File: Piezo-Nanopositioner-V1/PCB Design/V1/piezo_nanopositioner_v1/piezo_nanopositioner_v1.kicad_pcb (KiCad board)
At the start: 2 copper layers, 34 parts, among them J101 Conn_01x03_Pin, J401 Conn_01x10_Pin, J402 RF2-04A-T-00-50-G, U401 TL431AIDBZR, U402 DAC0800LCM, U403 TDA2050

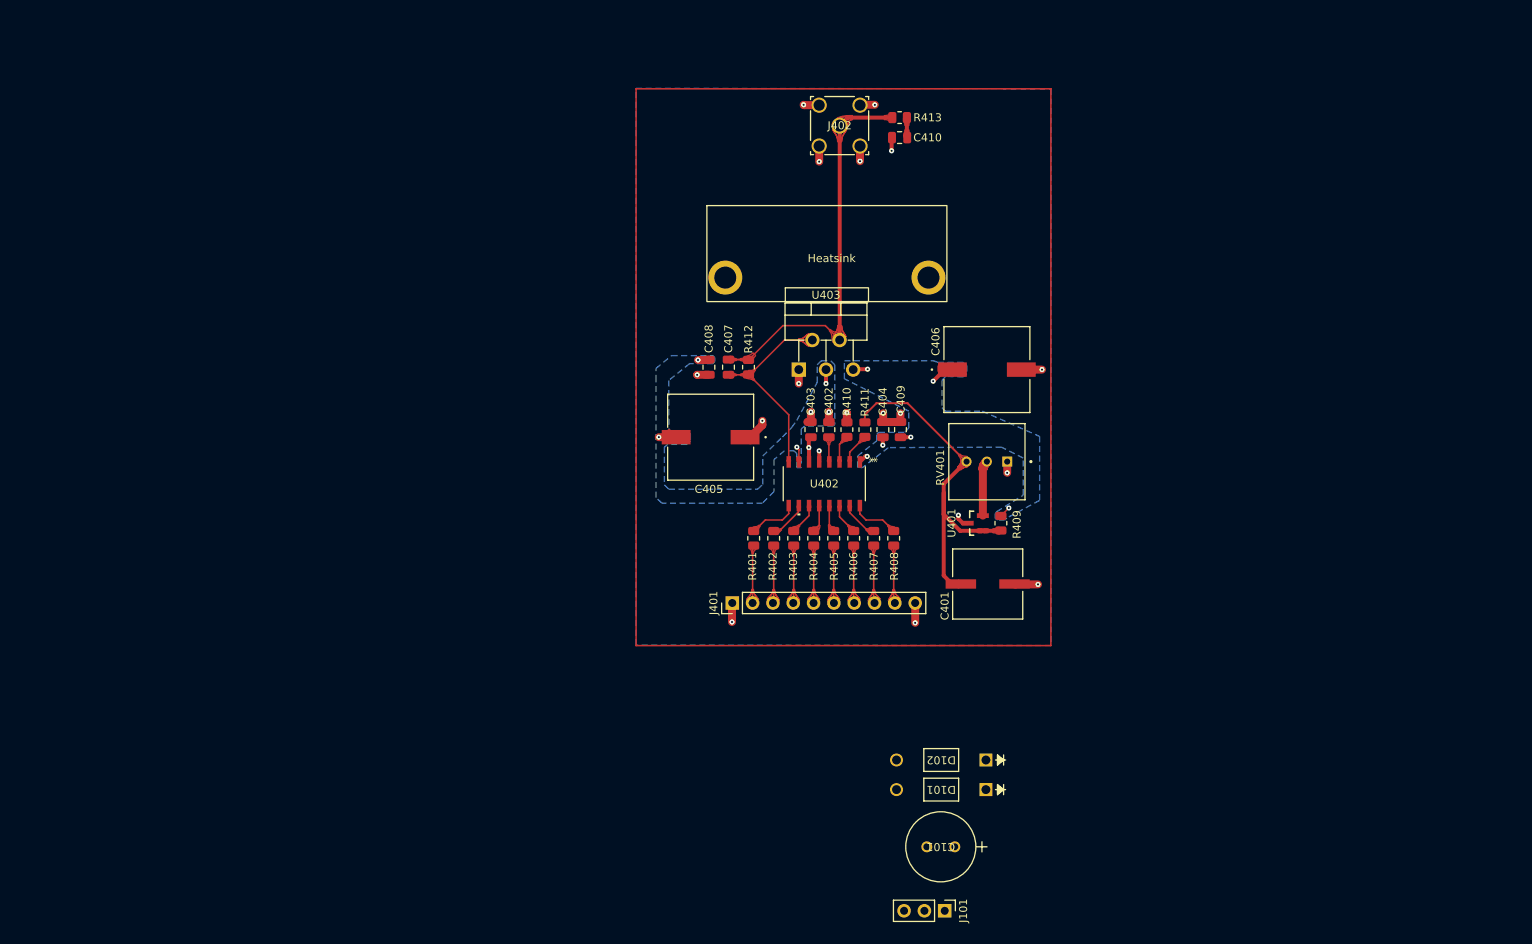
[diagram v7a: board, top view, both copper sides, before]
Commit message: Added 3d model files for component. Finished connecting the fill zones. Added mounting holes. Added pictures of pcb and layout.
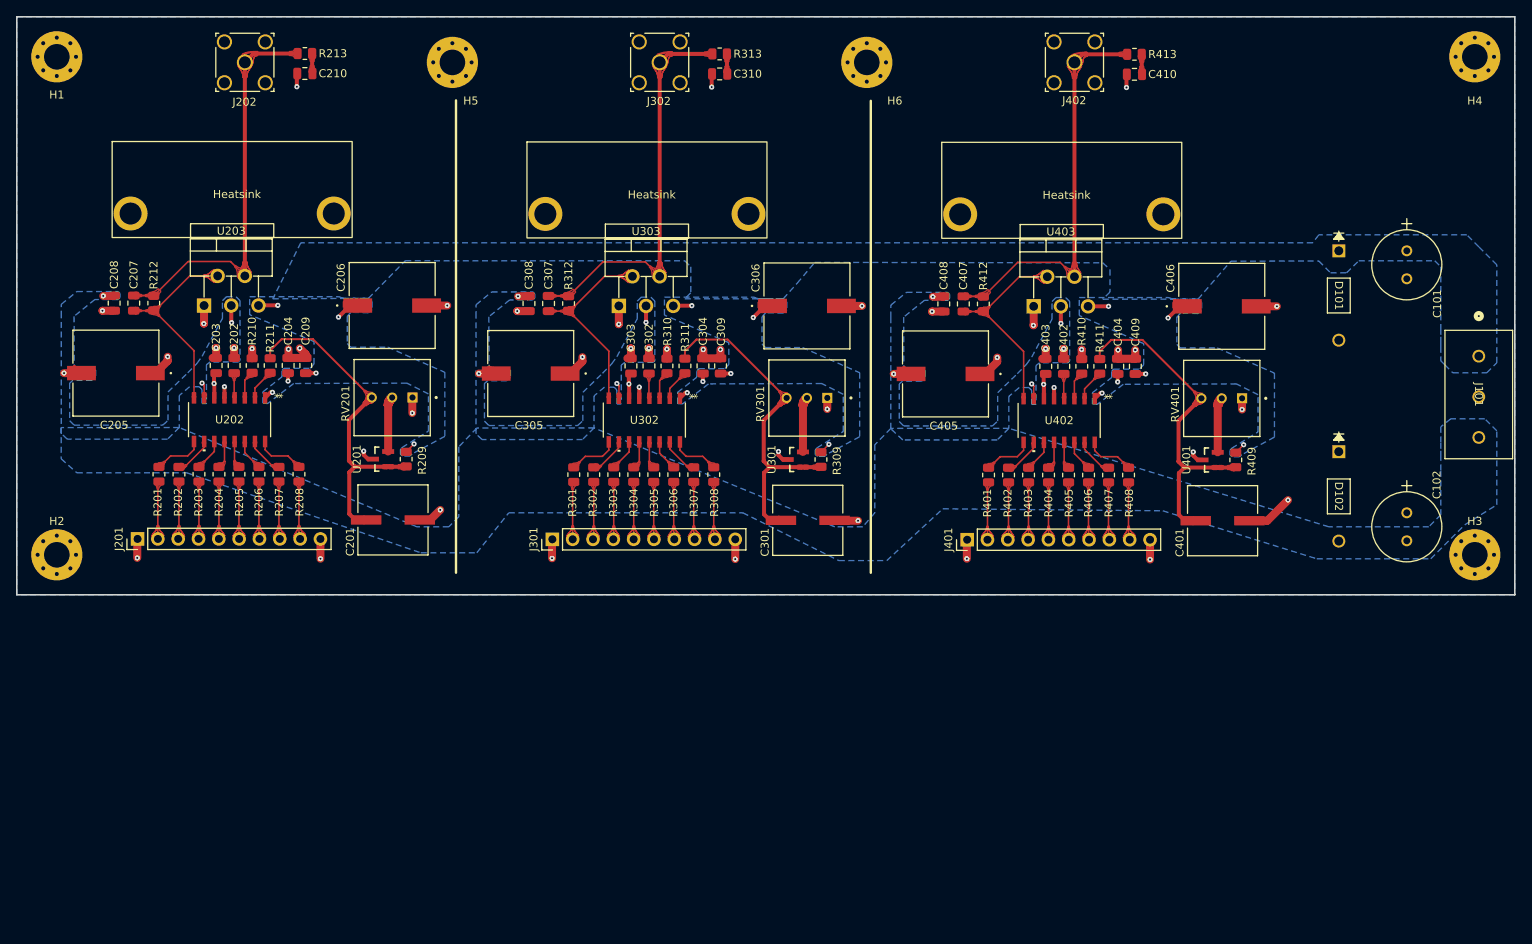
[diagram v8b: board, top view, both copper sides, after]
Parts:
- removed the Heatsink at (171.5, 76.1)
- added C102: 100uF 50V, Capacitor_THT:CAP_YX_8X11P5_RUB, F.Cu at (244.0, 105.5)
- added C201: 47u, Capacitor_SMD:CAP_EEFC_E_PAN, F.Cu at (117.3, 106.4)
- added C202: 10n, Capacitor_SMD:C_0805_2012Metric, F.Cu at (97.4, 87.1)
- added C203: 100n, Capacitor_SMD:C_0805_2012Metric, F.Cu at (95.2, 87.1)
- added C204: 100n, Capacitor_SMD:C_0805_2012Metric, F.Cu at (104.2, 87.1)
- added C205: 470u, Capacitor_THT:CAP_ZSU_G12_PAN, F.Cu at (82.6, 88.0)
- added C206: 470u, Capacitor_THT:CAP_ZSU_G12_PAN, F.Cu at (117.2, 79.6)
- added C207: 68p, Capacitor_SMD:C_0805_2012Metric, F.Cu at (84.9, 79.3)
- added C208: 100n, Capacitor_SMD:C_0805_2012Metric, F.Cu at (82.4, 79.3)
- added C209: 100n, Capacitor_SMD:C_0805_2012Metric, F.Cu at (106.4, 87.1)
- added C210: 4.7n, Capacitor_SMD:C_0805_2012Metric, F.Cu at (106.3, 50.6)
- added C301: 47u, Capacitor_SMD:CAP_EEFC_E_PAN, F.Cu at (169.1, 106.4)
- added C302: 10n, Capacitor_SMD:C_0805_2012Metric, F.Cu at (149.3, 87.1)
- added C303: 100n, Capacitor_SMD:C_0805_2012Metric, F.Cu at (147.0, 87.1)
- added C304: 100n, Capacitor_SMD:C_0805_2012Metric, F.Cu at (156.0, 87.1)
- added C305: 470u, Capacitor_THT:CAP_ZSU_G12_PAN, F.Cu at (134.5, 88.1)
- added C306: 470u, Capacitor_THT:CAP_ZSU_G12_PAN, F.Cu at (169.0, 79.6)
- added C307: 68p, Capacitor_SMD:C_0805_2012Metric, F.Cu at (136.7, 79.3)
- added C308: 100n, Capacitor_SMD:C_0805_2012Metric, F.Cu at (134.3, 79.3)
- added C309: 100n, Capacitor_SMD:C_0805_2012Metric, F.Cu at (158.2, 87.1)
- added C310: 4.7n, Capacitor_SMD:C_0805_2012Metric, F.Cu at (158.1, 50.6)
- added H1: MountingHole, MountingHole:MountingHole_3.2mm_M3_Pad_Via, F.Cu at (75.2, 48.5)
- added H2: MountingHole, MountingHole:MountingHole_3.2mm_M3_Pad_Via, F.Cu at (75.2, 110.8)
- added H3: MountingHole, MountingHole:MountingHole_3.2mm_M3_Pad_Via, F.Cu at (252.5, 110.8)
- added H4: MountingHole, MountingHole:MountingHole_3.2mm_M3_Pad_Via, F.Cu at (252.5, 48.5)
- added H5: MountingHole, MountingHole:MountingHole_3.2mm_M3_Pad_Via, F.Cu at (124.7, 49.2)
- added H6: MountingHole, MountingHole:MountingHole_3.2mm_M3_Pad_Via, F.Cu at (176.5, 49.2)
- added Heatsink: V6560Y, V6560Y:V6560Y, F.Cu at (200.9, 68.2)
- added Heatsink: V6560Y, V6560Y:V6560Y, F.Cu at (97.2, 68.1)
- added Heatsink: V6560Y, V6560Y:V6560Y, F.Cu at (149.0, 68.1)
- added J201: Conn_01x10_Pin, Connector_PinHeader_2.54mm:PinHeader_1x10_P2.54mm_Vertical, F.Cu at (85.3, 108.8)
- added J202: RF2-04A-T-00-50-G, RF:CONN_RF2-04A-T-00-50-G_ADM, F.Cu at (98.8, 49.2)
- added J301: Conn_01x10_Pin, Connector_PinHeader_2.54mm:PinHeader_1x10_P2.54mm_Vertical, F.Cu at (137.2, 108.8)
- added J302: RF2-04A-T-00-50-G, RF:CONN_RF2-04A-T-00-50-G_ADM, F.Cu at (150.6, 49.2)
- added R201: 100R, Resistor_SMD:R_0805_2012Metric, F.Cu at (88.0, 100.7)
- added R202: 100R, Resistor_SMD:R_0805_2012Metric, F.Cu at (90.5, 100.7)
- added R203: 100R, Resistor_SMD:R_0805_2012Metric, F.Cu at (93.0, 100.7)
- added R204: 100R, Resistor_SMD:R_0805_2012Metric, F.Cu at (95.5, 100.7)
- added R205: 100R, Resistor_SMD:R_0805_2012Metric, F.Cu at (98.0, 100.7)
- added R206: 100R, Resistor_SMD:R_0805_2012Metric, F.Cu at (100.5, 100.7)
- added R207: 100R, Resistor_SMD:R_0805_2012Metric, F.Cu at (103.0, 100.7)
- added R208: 100R, Resistor_SMD:R_0805_2012Metric, F.Cu at (105.5, 100.7)
- added R209: 1k, Resistor_SMD:R_0805_2012Metric, F.Cu at (118.9, 98.8)
- added R210: 5k, Resistor_SMD:R_0805_2012Metric, F.Cu at (99.7, 87.1)
- added R211: 5k, Resistor_SMD:R_0805_2012Metric, F.Cu at (101.9, 87.1)
- added R212: 15k, Resistor_SMD:R_0805_2012Metric, F.Cu at (87.4, 79.3)
- added R213: 10R, Resistor_SMD:R_0805_2012Metric, F.Cu at (106.3, 48.1)
- added R301: 100R, Resistor_SMD:R_0805_2012Metric, F.Cu at (139.9, 100.7)
- added R302: 100R, Resistor_SMD:R_0805_2012Metric, F.Cu at (142.4, 100.7)
- added R303: 100R, Resistor_SMD:R_0805_2012Metric, F.Cu at (144.9, 100.7)
- added R304: 100R, Resistor_SMD:R_0805_2012Metric, F.Cu at (147.4, 100.7)
- added R305: 100R, Resistor_SMD:R_0805_2012Metric, F.Cu at (149.9, 100.7)
- added R306: 100R, Resistor_SMD:R_0805_2012Metric, F.Cu at (152.4, 100.7)
- added R307: 100R, Resistor_SMD:R_0805_2012Metric, F.Cu at (154.9, 100.7)
- added R308: 100R, Resistor_SMD:R_0805_2012Metric, F.Cu at (157.4, 100.7)
- added R309: 1k, Resistor_SMD:R_0805_2012Metric, F.Cu at (170.8, 98.8)
- added R310: 5k, Resistor_SMD:R_0805_2012Metric, F.Cu at (151.5, 87.1)
- added R311: 5k, Resistor_SMD:R_0805_2012Metric, F.Cu at (153.8, 87.1)
- added R312: 15k, Resistor_SMD:R_0805_2012Metric, F.Cu at (139.2, 79.3)
- added R313: 10R, Resistor_SMD:R_0805_2012Metric, F.Cu at (158.1, 48.1)
- added RV201: 10k, Potentiometer_THT:TRIM_COM-09806, F.Cu at (117.2, 91.1)
- added RV301: 10k, Potentiometer_THT:TRIM_COM-09806, F.Cu at (169.0, 91.1)
- added U201: TL431AIDBZR, TL431AIDBZR:DBZ0003A_N, F.Cu at (115.7, 98.8)
- added U202: DAC0800LCM, DAC0800LCM_SMT:M16A_TEX, F.Cu at (96.8, 93.9)
- added U203: TDA2050, Package_TO_SOT_THT:TO-220-5_P3.4x3.7mm_StaggerOdd_Lead3.8mm_Vertical, F.Cu at (93.7, 79.6)
- added U301: TL431AIDBZR, TL431AIDBZR:DBZ0003A_N, F.Cu at (167.6, 98.8)
- added U302: DAC0800LCM, DAC0800LCM_SMT:M16A_TEX, F.Cu at (148.7, 93.9)
- added U303: TDA2050, Package_TO_SOT_THT:TO-220-5_P3.4x3.7mm_StaggerOdd_Lead3.8mm_Vertical, F.Cu at (145.5, 79.6)
- J101: footprint Connector_PinHeader_2.54mm:PinHeader_1x03_P2.54mm_Vertical -> Molex Connector:CONN_39880-0303_MOL
- moved J101 96.2 mm to (253.0, 85.9)
- moved C101 93.5 mm to (244.0, 72.8), turned to -90 degrees
- moved D101 80.5 mm to (235.5, 72.8), turned to -90 degrees
- moved D102 58.6 mm to (235.5, 97.9), turned to -90 degrees
- moved C401 30.4 mm to (221.0, 106.5)
- moved C402 30.4 mm to (201.1, 87.2)
- moved C403 30.4 mm to (198.9, 87.2)
- moved C404 30.4 mm to (207.9, 87.2)
- moved C405 30.4 mm to (186.3, 88.1)
- moved C406 30.4 mm to (220.9, 79.7)
- moved C408 30.4 mm to (186.1, 79.4)
- moved C410 30.4 mm to (210.0, 50.7)
- moved J402 30.4 mm to (202.5, 49.2)
- moved R401 30.4 mm to (191.7, 100.8)
- moved R402 30.4 mm to (194.2, 100.8)
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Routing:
- net Net-(J402-Sig): track 50.3 -> 150.8 mm
- net /Z_DAC/VRef+: track 46.0 -> 130.8 mm
- net GND: track 40.7 -> 105.1 mm, vias 19 -> 45
- net Net-(U402-IOUT): track 25.4 -> 76.1 mm
- net -15V: track 10.9 -> 33.7 mm, vias 6 -> 18
- net +15V: track 10.4 -> 33.0 mm, vias 6 -> 18
- net Net-(J401-Pin_9): track 7.24 -> 21.7 mm
- net Net-(J401-Pin_2): track 7.23 -> 21.7 mm
- net Net-(J401-Pin_8): track 7.22 -> 21.7 mm
- net Net-(J401-Pin_3): track 7.21 -> 21.6 mm
- net Net-(J401-Pin_7): track 7.20 -> 21.6 mm
- net Net-(J401-Pin_4): track 7.20 -> 21.6 mm
- net Net-(J401-Pin_6): track 7.19 -> 21.6 mm
- net Net-(J401-Pin_5): track 7.18 -> 21.5 mm
- net Net-(U401-REF): track 6.96 -> 20.9 mm
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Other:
- board outline added: 187.2 x 72.2 mm
